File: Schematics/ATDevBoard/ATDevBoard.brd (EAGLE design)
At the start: 66.2 x 54.4 mm, 40 parts, among them U1 TINY85-DIP

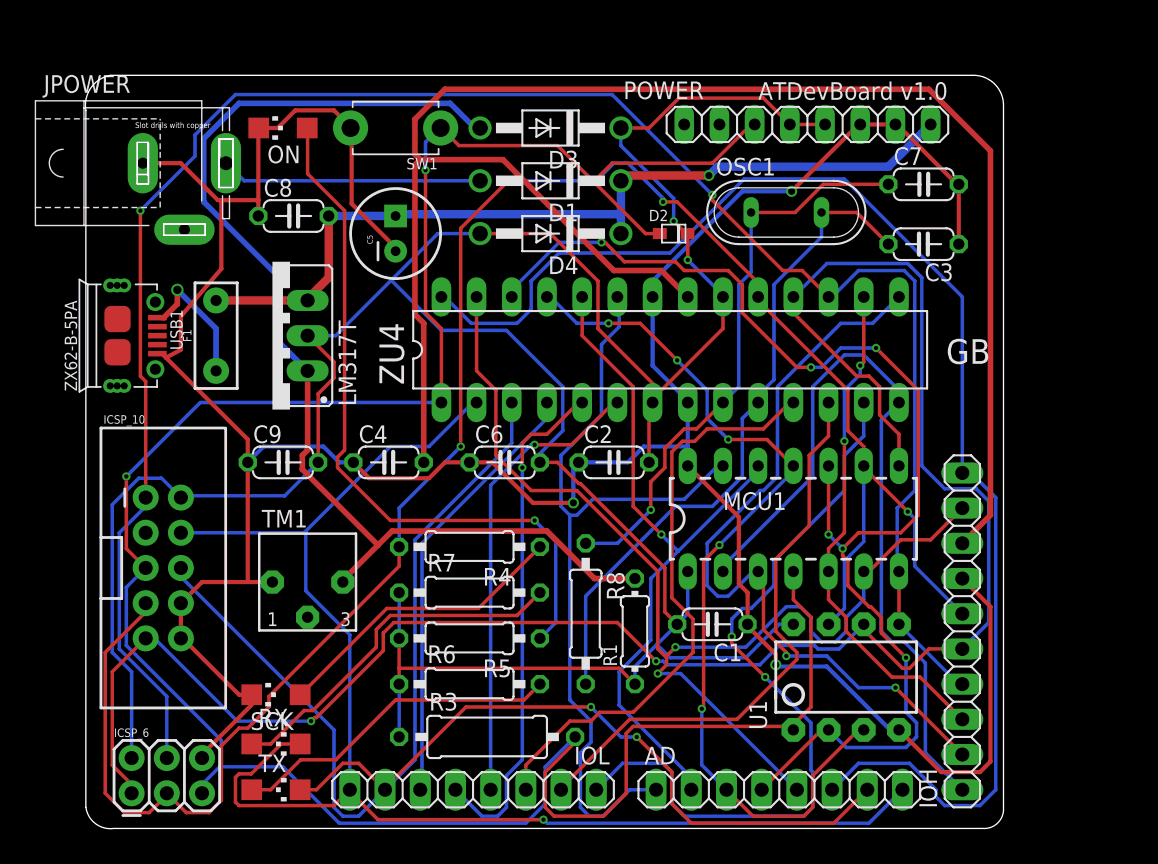
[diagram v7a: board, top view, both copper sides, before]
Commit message: Changed size of power header to 5, added label for all signals in/out
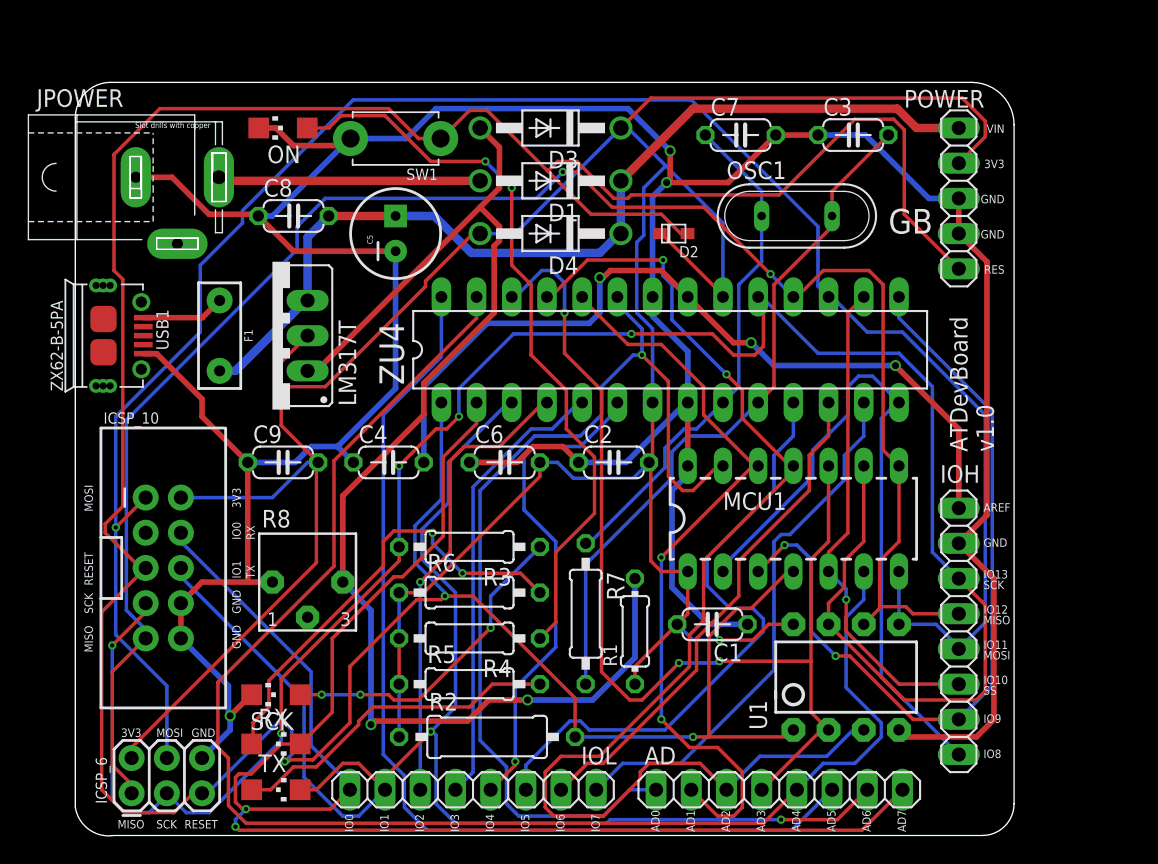
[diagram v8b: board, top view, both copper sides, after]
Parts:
- removed TM1: 2K, bourns:3362R
- added R2: 10K, rcl:0309/12
- IOH: device pinhead:1X10 -> pinhead:1X08
- POWER: value 8x1F-H8.5 -> 6x1F-H8.5; device SmartPrj:1X08 -> pinhead:1X05
- R3: value 10K -> 1K; device rcl:0309/12 -> rcl:0207/10
- R7: value 1K -> 1M
- R8: value 1M -> (none); device rcl:0207/10 -> bourns:3362R
- moved R8 20.2 mm to (16.5, 17.8), turned to 0 degrees
- moved R3 13.8 mm to (28.2, 20.3), turned to 180 degrees
- moved C7 13.7 mm to (47.8, 50.0)
- moved POWER 12.2 mm to (63.5, 45.5), turned to 90 degrees
- moved C3 9.37 mm to (55.9, 50.0), turned to 0 degrees
- moved R7 8.52 mm to (36.6, 15.5), turned to 270 degrees
- moved R4 6.60 mm to (28.2, 13.7)
- moved R6 6.60 mm to (28.2, 17.0)
- moved R5 3.30 mm to (28.2, 10.4), turned to 0 degrees
- moved JPOWER 1.14 mm to (7.11, 47.0)
- moved USB1 1.02 mm to (1.78, 35.6)
- moved OSC1 0.80 mm to (51.8, 44.2)
- moved SW1 0.76 mm to (22.9, 49.8)
- moved F1 0.25 mm to (10.2, 35.6), turned to 270 degrees
- moved IOH 0.25 mm to (63.5, 14.2)
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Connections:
- net +3V3: now also R2.1, R4.2, R5.1; no longer POWER.5, R3.1, R5.2, R7.1
- net AD4: no longer IOH.9
- net AD5: no longer IOH.10
- net GND: now also POWER.2, POWER.3, R8.1; no longer POWER.6, POWER.7, TM1.1
- net N$1: now also R8.3; no longer TM1.3
- net N$3: now also R4.1; no longer R5.1
- net N$35: now also R6.2; no longer R7.2
- net N$36: now also R5.2; no longer R6.2
- net N$4: now also R3.1; no longer R4.1
- net RESET: now also POWER.1, R2.2; no longer POWER.3, R3.2
- net SCK: now also R3.2; no longer R4.2
- net VIN: now also POWER.5; no longer POWER.8
- net XTAL1: now also R7.1; no longer R8.1
- net XTAL2: now also R7.2; no longer R8.2
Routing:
- net AREF: track 122.2 -> 59.5 mm, vias 0 -> 3
- net RESET: track 178.9 -> 239.9 mm, vias 2 -> 3
- net GND: track 224.3 -> 261.0 mm
- net AD4: track 78.9 -> 108.5 mm, vias 2 -> 0
- net AD5: track 99.0 -> 72.0 mm
- net AD2: track 65.5 -> 89.9 mm, vias 5 -> 2
- net IO0: track 103.4 -> 121.4 mm, vias 1 -> 2
- net IO7: track 55.5 -> 38.8 mm, vias 2 -> 0
- net N$1: track 80.7 -> 94.4 mm, vias 0 -> 2
- net AD0: track 58.9 -> 71.8 mm, vias 0 -> 1
- net SCK: track 143.9 -> 155.7 mm, vias 4 -> 5
- net AD3: track 89.6 -> 77.8 mm, vias 6 -> 3
- net MISO: track 140.1 -> 129.0 mm
- net VIN: track 62.3 -> 68.8 mm, vias 1 -> 0
- net N$35: track 26.1 -> 32.5 mm, vias 0 -> 2
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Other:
- board size 66.2 x 54.4 mm -> 67.7 x 54.4 mm
- board text added: "3V3"
- board text added: "AD0"
- board text added: "AD1"
- board text added: "AD2"
- board text added: "AD3"
- board text added: "AD4"
- board text added: "AD5"
- board text added: "AD6"
- board text added: "AD7"
- board text added: "AREF"
- board text added: "GND"
- board text added: "IO0"
- board text added: "IO1"
- board text added: "IO10"
- board text added: "IO11"
- board text added: "IO12"
- board text added: "IO13"
- board text added: "IO2"
- board text added: "IO3"
- board text added: "IO4"
- board text added: "IO5"
- board text added: "IO6"
- board text added: "IO7"
- board text added: "IO8"
- board text added: "IO9"
- board text added: "MISO"
- board text added: "MOSI"
- board text added: "RES"
- board text added: "RESET"
- board text added: "RX"
- board text added: "SCK"
- board text added: "SS"
- board text added: "TX"
- board text added: "VIN"
